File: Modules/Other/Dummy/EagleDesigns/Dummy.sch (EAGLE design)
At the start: 1 part

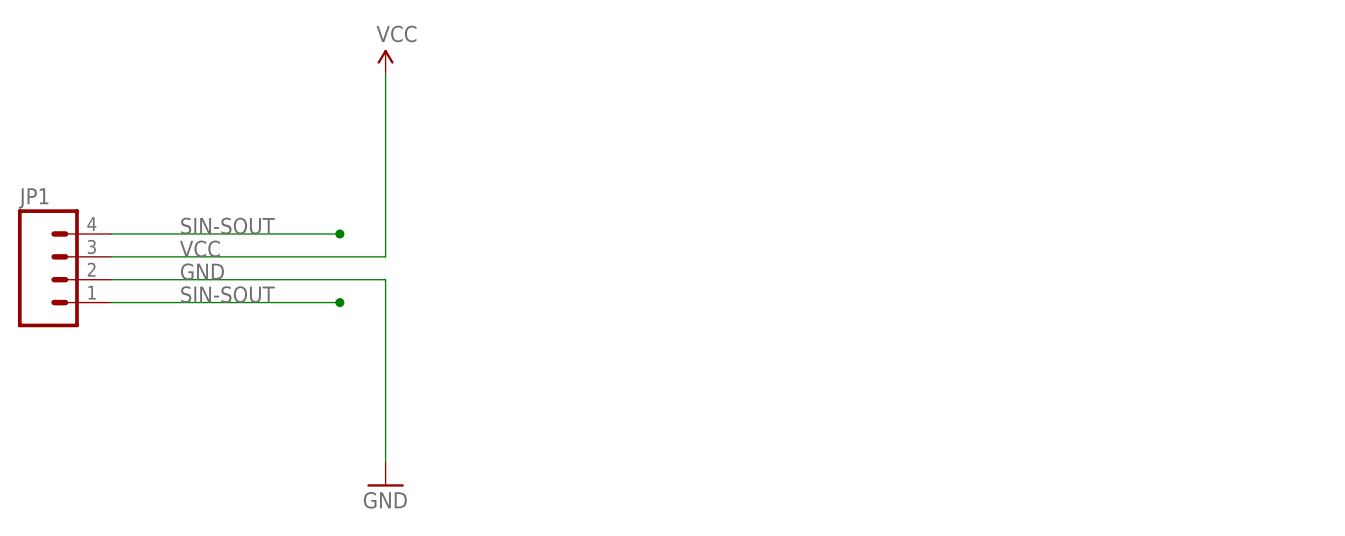
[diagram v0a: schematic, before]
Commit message: Added one single Board Layout for WireSEND, WireRECV, and Dummy module
it now has a small jumper that could be soldered in order to connect
SIN to SOUT.
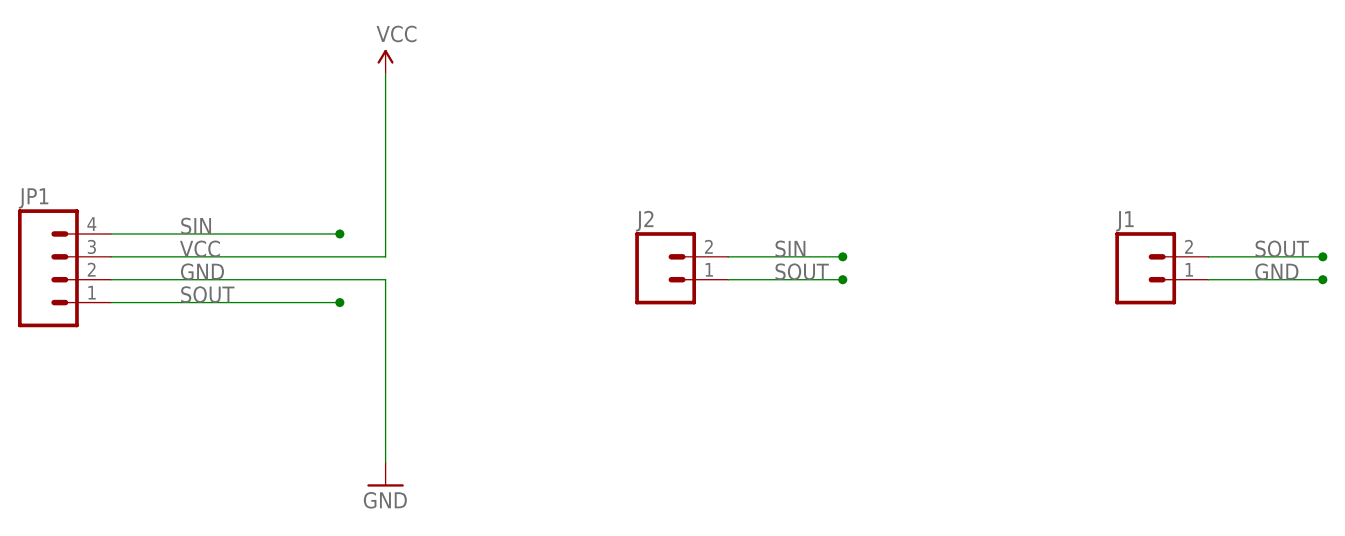
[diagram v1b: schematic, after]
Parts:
- added J1, J2: (no value), SparkFun-Connectors:M02PTH
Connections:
- removed net SIN-SOUT: JP1.1, JP1.4
- new net SIN: J2.2, JP1.4
- new net SOUT: J1.2, J2.1, JP1.1
- net GND: now also J1.1
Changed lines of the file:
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@@
 <part name="SUPPLY1" library="SparkFun-Aesthetics" deviceset="VCC" device=""/>
 <part name="GND1" library="SparkFun-Aesthetics" deviceset="GND" device=""/>
+<part name="J2" library="SparkFun-Connectors" deviceset="M02" device="PTH"/>
+<part name="J1" library="SparkFun-Connectors" deviceset="M02" device="PTH"/>
 </parts>
 <sheets>
@@
 <instance part="SUPPLY1" gate="G$1" x="40.64" y="27.94"/>
 <instance part="GND1" gate="1" x="40.64" y="-17.78"/>
+<instance part="J2" gate="G$1" x="71.12" y="5.08"/>
+<instance part="J1" gate="G$1" x="124.46" y="5.08"/>
 </instances>
 <busses>
@@
 <wire x1="40.64" y1="5.08" x2="40.64" y2="-15.24" width="0.1524" layer="91"/>
 </segment>
+<segment>
+<pinref part="J1" gate="G$1" pin="1"/>
+<wire x1="132.08" y1="5.08" x2="144.78" y2="5.08" width="0.1524" layer="91"/>
+<junction x="144.78" y="5.08"/>
+<label x="137.16" y="5.08" size="1.778" layer="95"/>
+</segment>
 </net>
-<net name="SIN-SOUT" class="0">
+<net name="SIN" class="0">
 <segment>
 <pinref part="JP1" gate="G$1" pin="4"/>
@@
 </segment>
 <segment>
+<pinref part="J2" gate="G$1" pin="2"/>
+<wire x1="78.74" y1="7.62" x2="91.44" y2="7.62" width="0.1524" layer="91"/>
+<junction x="91.44" y="7.62"/>
+<label x="83.82" y="7.62" size="1.778" layer="95"/>
+</segment>
+</net>
+<net name="SOUT" class="0">
+<segment>
 <pinref part="JP1" gate="G$1" pin="1"/>
 <wire x1="10.16" y1="2.54" x2="35.56" y2="2.54" width="0.1524" layer="91"/>
@@
 <junction x="35.56" y="2.54"/>
 </segment>
+<segment>
+<pinref part="J2" gate="G$1" pin="1"/>
+<wire x1="78.74" y1="5.08" x2="91.44" y2="5.08" width="0.1524" layer="91"/>
+<junction x="91.44" y="5.08"/>
+<label x="83.82" y="5.08" size="1.778" layer="95"/>
+</segment>
+<segment>
+<pinref part="J1" gate="G$1" pin="2"/>
+<wire x1="132.08" y1="7.62" x2="144.78" y2="7.62" width="0.1524" layer="91"/>
+<junction x="144.78" y="7.62"/>
+<label x="137.16" y="7.62" size="1.778" layer="95"/>
+</segment>
 </net>
